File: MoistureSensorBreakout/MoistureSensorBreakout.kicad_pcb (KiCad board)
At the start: 2 copper layers, 54.8 x 45 mm, 4 parts, among them J1 Conn_02x07_Odd_Even, J2 Conn_01x06, J3 Conn_01x05, J4 Conn_01x14

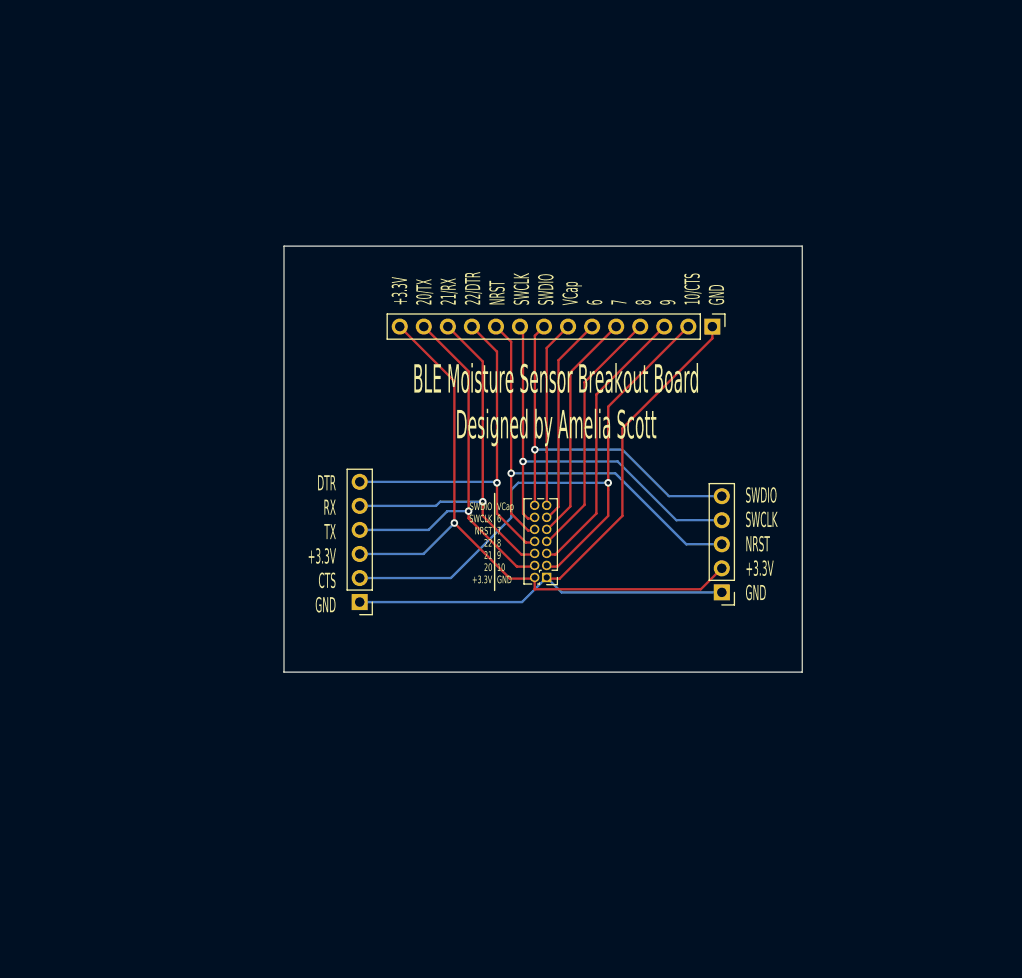
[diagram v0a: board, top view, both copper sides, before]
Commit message: New version of breakout / programming board
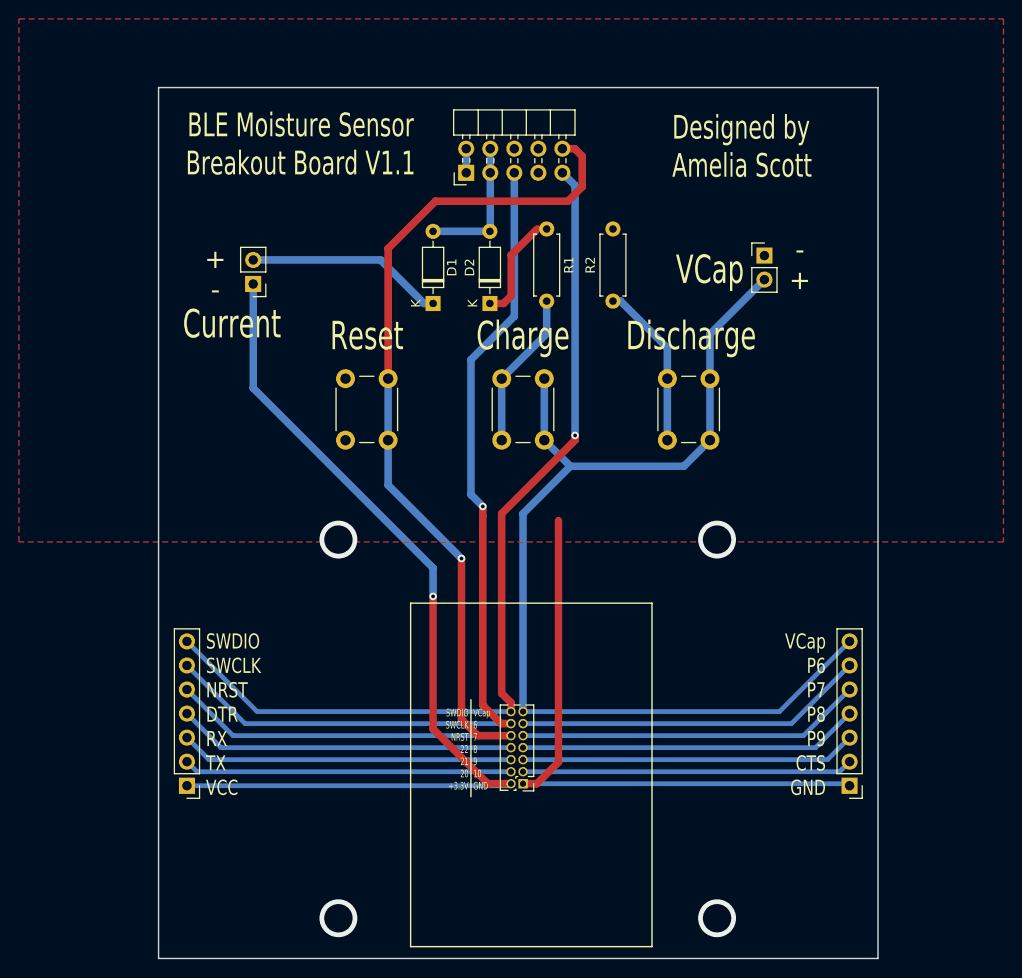
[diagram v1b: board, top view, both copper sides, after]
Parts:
- removed J4: Conn_01x14, Connector_PinHeader_2.54mm:PinHeader_1x14_P2.54mm_Vertical
- added D1: 1N4148, Diode_THT:D_DO-35_SOD27_P7.62mm_Horizontal, F.Cu at (138.0, 71.1)
- added D2: 1N4148, Diode_THT:D_DO-35_SOD27_P7.62mm_Horizontal, F.Cu at (144.0, 71.1)
- added I1: Conn_01x02, Connector_PinHeader_2.54mm:PinHeader_1x02_P2.54mm_Vertical, F.Cu at (119.0, 69.0)
- added R1: 10, Resistor_THT:R_Axial_DIN0207_L6.3mm_D2.5mm_P7.62mm_Horizontal, F.Cu at (150.0, 63.2)
- added R2: 10, Resistor_THT:R_Axial_DIN0207_L6.3mm_D2.5mm_P7.62mm_Horizontal, F.Cu at (157.0, 70.8)
- added SWD1: Conn_02x05_Odd_Even, Connector_PinHeader_2.54mm:PinHeader_2x05_P2.54mm_Horizontal, F.Cu at (141.5, 57.2)
- added SW_CAP_CHARGE1: SW_Push, Button_Switch_THT:SW_PUSH_6mm, F.Cu at (145.2, 85.5)
- added SW_CAP_DISCHARGE1: SW_Push, Button_Switch_THT:SW_PUSH_6mm, F.Cu at (167.2, 79.0)
- added SW_RST1: SW_Push, Button_Switch_THT:SW_PUSH_6mm, F.Cu at (133.2, 79.0)
- added VCAP: Conn_01x02, Connector_PinHeader_2.54mm:PinHeader_1x02_P2.54mm_Vertical, F.Cu at (173.0, 66.0)
- J2: value Conn_01x06 -> Conn_01x07; footprint Connector_PinHeader_2.54mm:PinHeader_1x06_P2.54mm_Vertical -> Connector_PinHeader_2.54mm:PinHeader_1x07_P2.54mm_Vertical
- J3: value Conn_01x05 -> Conn_01x07; footprint Connector_PinHeader_2.54mm:PinHeader_1x05_P2.54mm_Vertical -> Connector_PinHeader_2.54mm:PinHeader_1x07_P2.54mm_Vertical
- moved J3 60.1 mm to (112.0, 122.0)
- moved J2 55.3 mm to (182.0, 122.0)
- moved J1 21.9 mm to (147.5, 121.8)
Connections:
- J1 pad 2: +3.3v -> SensorVCC
- J2 pad 3: +3.3v -> P9
- J2 pad 4: TX -> P8
- J2 pad 5: RX -> P7
- J2 pad 6: DTR -> P6
- J3 pad 1: GND -> SensorVCC
- J3 pad 2: +3.3v -> TX
- J3 pad 3: NRST -> RX
- J3 pad 4: SWCLK -> DTR
- J3 pad 5: SWDIO -> NRST
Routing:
- net SensorVCC: track 0.00 -> 99.8 mm, vias 0 -> 1
- net VCap: track 19.9 -> 111.2 mm
- net NRST: track 49.0 -> 124.0 mm
- net +3.3v: track 67.4 -> 0.00 mm, vias 1 -> 0
- net SWDIO: track 41.2 -> 98.4 mm
- net SWCLK: track 44.9 -> 99.2 mm
- net CTS: track 64.3 -> 34.9 mm, vias 1 -> 0
- net Net-(D1-Pad1): track 0.00 -> 20.9 mm
- net Net-(R2-Pad1): track 0.00 -> 17.5 mm
- net Net-(R1-Pad2): track 0.00 -> 16.7 mm
- net P6: track 22.2 -> 37.0 mm
- net +3.3V: track 0.00 -> 14.7 mm
- net P7: track 24.5 -> 36.5 mm
- net Net-(D2-Pad1): track 0.00 -> 10.8 mm
- net GND: track 74.6 -> 64.8 mm
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- added copper zone on F.Cu, net GND
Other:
- board size 54.8 x 45 mm -> 76 x 92 mm
- board text added: "+ -"
- board text added: "- +"
- board text added: "BLE Moisture Sensor Breakout Board V1.1"
- board text added: "Charge"
- board text added: "Current"
- board text added: "Designed by Amelia Scott"
- board text added: "Discharge"
- board text added: "Reset"
- board text added: "SWDIO SWCLK NRST DTR RX TX VCC"
- board text added: "VCap"
- board text added: "VCap P6 P7 P8 P9 CTS GND"
- board text removed: "+3.3V 20/TX 21/RX 22/DTR NRST SWCLK SWDIO VCap 6 7 8 9 10/CTS GND"
- board text removed: "BLE Moisture Sensor Breakout Board Designed by Amelia Scott"
- board text removed: "DTR RX TX +3.3V CTS GND"
- board text removed: "SWDIO SWCLK NRST +3.3V GND"
